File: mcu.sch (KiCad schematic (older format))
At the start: 30 parts, among them Q3 MMBT3904-7-F, SW1 PTS645VL39-2, U4 CAT24C32, U5 STM32F765VIT6, X1 ECS-TXO-3225-200-TR

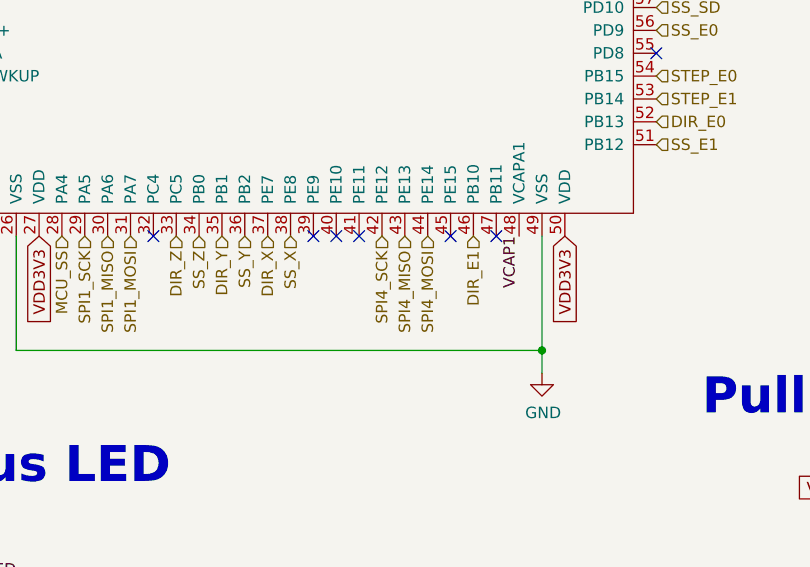
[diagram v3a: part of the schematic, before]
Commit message: Connected TMC DIAG pins to MCU
We had some pins free, so I decided to connect them, so that we
don't need to use the ENDSTOP OVER SPI feature.
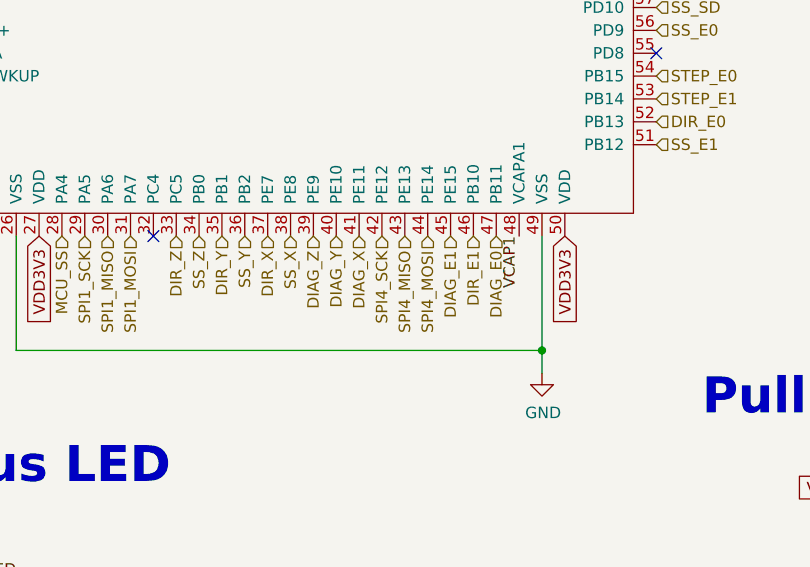
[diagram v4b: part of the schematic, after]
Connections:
- net DIAG_Z: now reaches U5.39 (PE9)
- net DIAG_Y: now reaches U5.40 (PE10)
- net DIAG_X: now reaches U5.41 (PE11)
- net DIAG_E1: now reaches U5.45 (PE15)
- net DIAG_E0: now reaches U5.47 (PB11)
- no-connect marks 25 -> 20
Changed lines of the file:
@@
 SPI1_MOSI
 NoConn ~ 6150 4600
-NoConn ~ 6850 4600
-NoConn ~ 6950 4600
 Text HLabel 6350 4600 3    50   Input ~ 0
 SS_Z
@@
 Text HLabel 7250 4600 3    50   Input ~ 0
 SPI4_MISO
-NoConn ~ 7450 4600
 Text HLabel 7350 4600 3    50   Input ~ 0
 SPI4_MOSI
@@
 DIR_X
 NoConn ~ 8350 3800
-NoConn ~ 7650 4600
 Text HLabel 8350 3500 2    50   Input ~ 0
 SD_DETECT
-NoConn ~ 7050 4600
 Text HLabel 5150 2000 0    50   Input ~ 0
 X_MIN
@@
 Text HLabel 5150 1800 0    50   Input ~ 0
 Z_MIN
-$Comp
-L heteromycin:STM32F765VIT6 U5
-U 1 1 5AD0AB9A
-P 6750 3000
-F 0 "U5" H 6750 3000 50  0000 L CNN
-F 1 "STM32F765VIT6" H 6500 2900 50  0000 L CNN
-F 2 "heteromycin:TQFP-100_14x14mm_P0.5mm" H 6750 3000 50  0001 C CNN
-F 3 "http://www.st.com/en/microcontrollers/stm32f765vi.html" H 6750 3000 50  0001 C CNN
-	1    6750 3000
-	1    0    0    -1
-$EndComp
 Text HLabel 6850 1400 1    50   Input ~ 0
 D1
@@
 	2000 2850 1900 2850
 NoConn ~ 7850 1400
+$Comp
+L heteromycin:STM32F765VIT6 U5
+U 1 1 5AD0AB9A
+P 6750 3000
+F 0 "U5" H 6750 3000 50  0000 L CNN
+F 1 "STM32F765VIT6" H 6500 2900 50  0000 L CNN
+F 2 "heteromycin:TQFP-100_14x14mm_P0.5mm" H 6750 3000 50  0001 C CNN
+F 3 "http://www.st.com/en/microcontrollers/stm32f765vi.html" H 6750 3000 50  0001 C CNN
+	1    6750 3000
+	1    0    0    -1
+$EndComp
+Text HLabel 6850 4600 3    50   Input ~ 0
+DIAG_Z
+Text HLabel 6950 4600 3    50   Input ~ 0
+DIAG_Y
+Text HLabel 7050 4600 3    50   Input ~ 0
+DIAG_X
+Text HLabel 7450 4600 3    50   Input ~ 0
+DIAG_E1
+Text HLabel 7650 4600 3    50   Input ~ 0
+DIAG_E0
 $EndSCHEMATC

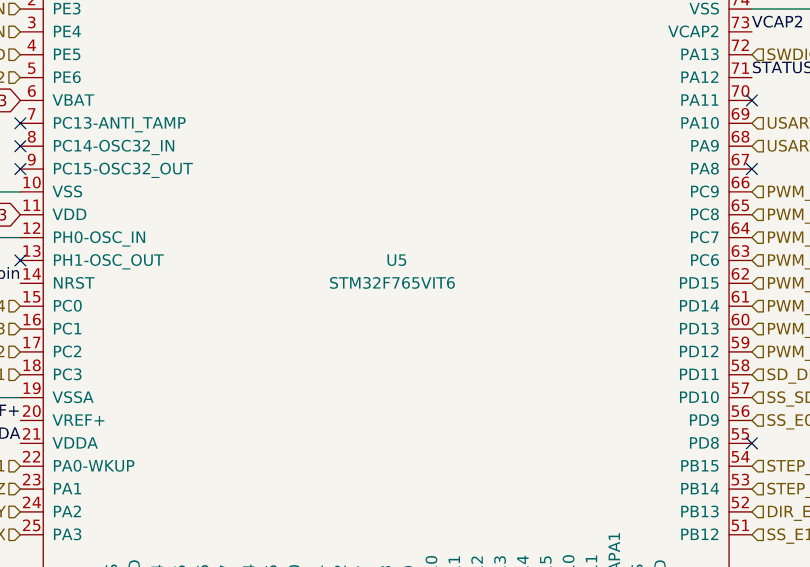
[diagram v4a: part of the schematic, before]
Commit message: Update the MCU from STM32F765VI to STM32H743VI
More speed, more RAM. Only loose the compability to flash over
USART3. Flashing over USART1/I2C/SPI is still possible.
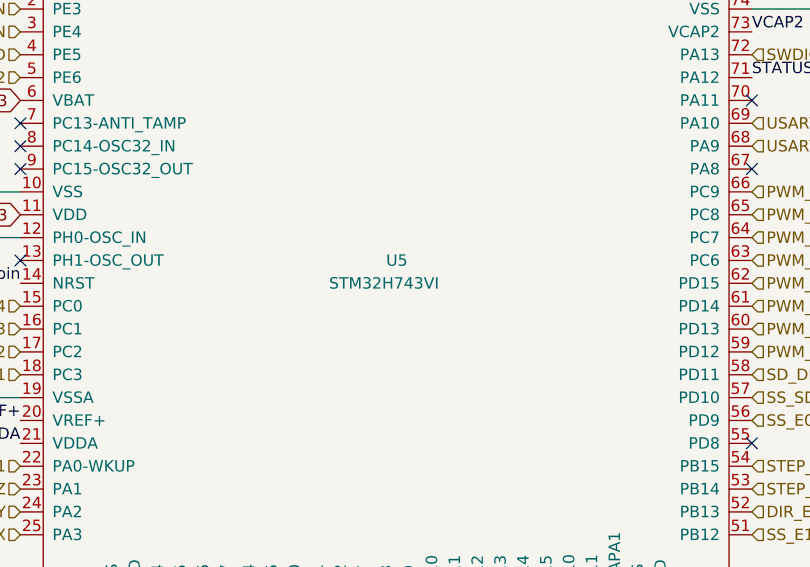
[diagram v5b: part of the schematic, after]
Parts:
- U5: value STM32F765VIT6 -> STM32H743VI
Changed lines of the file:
@@
 P 6750 3000
 F 0 "U5" H 6750 3000 50  0000 L CNN
-F 1 "STM32F765VIT6" H 6500 2900 50  0000 L CNN
+F 1 "STM32H743VI" H 6500 2900 50  0000 L CNN
 F 2 "heteromycin:TQFP-100_14x14mm_P0.5mm" H 6750 3000 50  0001 C CNN
-F 3 "http://www.st.com/en/microcontrollers/stm32f765vi.html" H 6750 3000 50  0001 C CNN
+F 3 "https://www.st.com/en/microcontrollers/stm32h743vi.html" H 6750 3000 50  0001 C CNN
 	1    6750 3000
 	1    0    0    -1

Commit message: Improve Readability
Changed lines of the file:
@@
-$EndComp
-$Comp
-L power:GND #PWR043
-U 1 1 5AF5BF00
-P 4450 3600
-F 0 "#PWR043" H 4450 3350 50  0001 C CNN
-F 1 "GND" V 4455 3472 50  0000 R CNN
-F 2 "" H 4450 3600 50  0001 C CNN
-F 3 "" H 4450 3600 50  0001 C CNN
-	1    4450 3600
-	0    1    1    0
 $EndComp
 $Comp
@@
 $EndComp
 $Comp
-L power:GND #PWR047
-U 1 1 5AF5E7FC
-P 9300 1900
-F 0 "#PWR047" H 9300 1650 50  0001 C CNN
-F 1 "GND" H 9300 1750 50  0000 C CNN
-F 2 "" H 9300 1900 50  0001 C CNN
-F 3 "" H 9300 1900 50  0001 C CNN
-	1    9300 1900
-	0    -1   -1   0
-$EndComp
-$Comp
 L power:GND #PWR046
 U 1 1 5AF5F2E4
@@
 	1    1550 2850
 	1    0    0    -1
-$EndComp
-$Comp
-L power:GND #PWR032
-U 1 1 5AF616AA
-P 1100 2850
-F 0 "#PWR032" H 1100 2600 50  0001 C CNN
-F 1 "GND" H 1105 2677 50  0000 C CNN
-F 2 "" H 1100 2850 50  0001 C CNN
-F 3 "" H 1100 2850 50  0001 C CNN
-	1    1100 2850
-	0    1    1    0
 $EndComp
 Wire Wire Line
@@
 	1450 6500 1800 6500
 Connection ~ 1800 6500
-Connection ~ 1100 2850
 Text GLabel 8350 1800 2    50   Input ~ 0
 VDD3V3
@@
 Wire Wire Line
 	1900 3200 1900 2850
-$Comp
-L power:GND #PWR031
-U 1 1 5AFDE2A1
-P 950 7450
-F 0 "#PWR031" H 950 7200 50  0001 C CNN
-F 1 "GND" H 955 7277 50  0000 C CNN
-F 2 "" H 950 7450 50  0001 C CNN
-F 3 "" H 950 7450 50  0001 C CNN
-	1    950  7450
-	0    1    1    0
-$EndComp
 Text HLabel 4050 2650 2    50   Input ~ 0
 BOOT
@@
 	1    1900 4350
 	1    0    0    -1
-$EndComp
-$Comp
-L power:GND #PWR?
-U 1 1 5BC1FDFA
-P 1300 4250
-AR Path="/5BC1FDFA" Ref="#PWR?"  Part="1"
-AR Path="/5BC4AC32/5BC1FDFA" Ref="#PWR?"  Part="1"
-AR Path="/5BC1C8A4/5BC1FDFA" Ref="#PWR033"  Part="1"
-F 0 "#PWR033" H 1300 4000 50  0001 C CNN
-F 1 "GND" H 1300 4100 50  0000 C CNN
-F 2 "" H 1300 4250 50  0000 C CNN
-F 3 "" H 1300 4250 50  0000 C CNN
-	1    1300 4250
-	0    1    1    0
 $EndComp
 $Comp
@@
 	5650 1400 5650 850
 Wire Wire Line
-	4450 3600 4500 3600
-Wire Wire Line
-	4500 3600 4500 2700
-Wire Wire Line
 	4500 2700 5150 2700
-Connection ~ 4500 3600
 Wire Wire Line
 	4500 3600 5150 3600
@@
 Wire Wire Line
 	950  7150 1150 7150
-Wire Wire Line
-	950  7450 1150 7450
 Connection ~ 1150 7150
 Wire Wire Line
 	1150 7150 1600 7150
-Connection ~ 1150 7450
 Wire Wire Line
 	1150 7450 1600 7450
@@
 Text HLabel 7650 4600 3    50   Input ~ 0
 DIAG_E0
+Wire Wire Line
+	4500 3600 4500 2700
+$Comp
+L power:GND #PWR0138
+U 1 1 5C45B9BC
+P 4500 3600
+F 0 "#PWR0138" H 4500 3350 50  0001 C CNN
+F 1 "GND" H 4505 3427 50  0000 C CNN
+F 2 "" H 4500 3600 50  0001 C CNN
+F 3 "" H 4500 3600 50  0001 C CNN
+	1    4500 3600
+	1    0    0    -1
+$EndComp
+Connection ~ 4500 3600
+$Comp
+L power:GND #PWR0139
+U 1 1 5C45C692
+P 1100 3200
+F 0 "#PWR0139" H 1100 2950 50  0001 C CNN
+F 1 "GND" H 1105 3027 50  0000 C CNN
+F 2 "" H 1100 3200 50  0001 C CNN
+F 3 "" H 1100 3200 50  0001 C CNN
+	1    1100 3200
+	1    0    0    -1
+$EndComp
+Connection ~ 1100 3200
+$Comp
+L power:GND #PWR0140
+U 1 1 5C45CCF1
+P 1300 4550
+F 0 "#PWR0140" H 1300 4300 50  0001 C CNN
+F 1 "GND" H 1305 4377 50  0000 C CNN
+F 2 "" H 1300 4550 50  0001 C CNN
+F 3 "" H 1300 4550 50  0001 C CNN
+	1    1300 4550
+	1    0    0    -1
+$EndComp
+Connection ~ 1300 4550
+$Comp
+L power:GND #PWR0141
+U 1 1 5C45CE8D
+P 1150 7450
+F 0 "#PWR0141" H 1150 7200 50  0001 C CNN
+F 1 "GND" H 1155 7277 50  0000 C CNN
+F 2 "" H 1150 7450 50  0001 C CNN
+F 3 "" H 1150 7450 50  0001 C CNN
+	1    1150 7450
+	1    0    0    -1
+$EndComp
+Connection ~ 1150 7450
+$Comp
+L power:GND #PWR0142
+U 1 1 5C45D233
+P 9300 1900
+F 0 "#PWR0142" H 9300 1650 50  0001 C CNN
+F 1 "GND" H 9305 1727 50  0000 C CNN
+F 2 "" H 9300 1900 50  0001 C CNN
+F 3 "" H 9300 1900 50  0001 C CNN
+	1    9300 1900
+	1    0    0    -1
+$EndComp
 $EndSCHEMATC

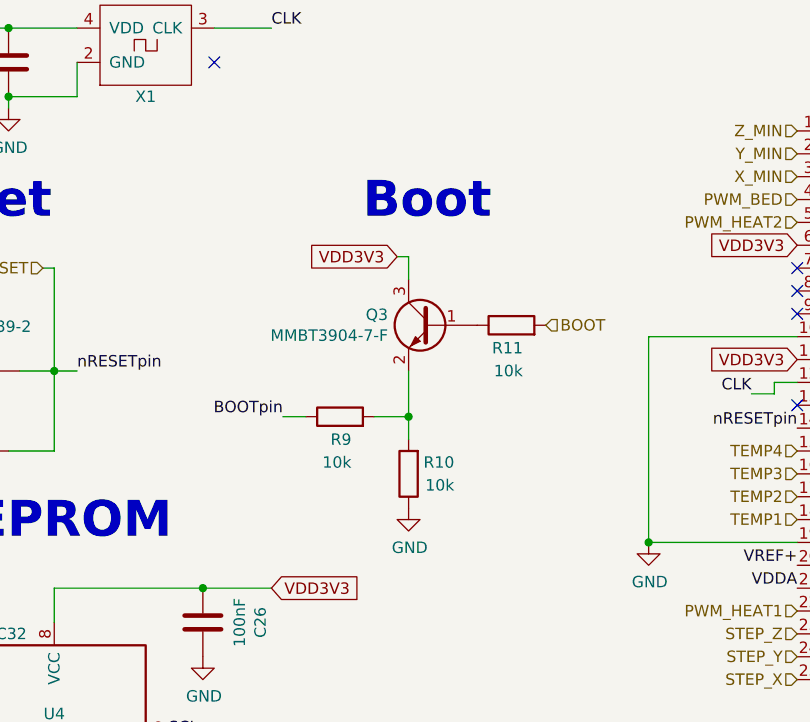
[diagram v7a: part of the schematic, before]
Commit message: Changed boot pin drive interface
Changed the boot pin to a direct connection since the current design depends on a existing raspberry to work. Used a 10kOhms resistor since that's the one used in the development board made by ST
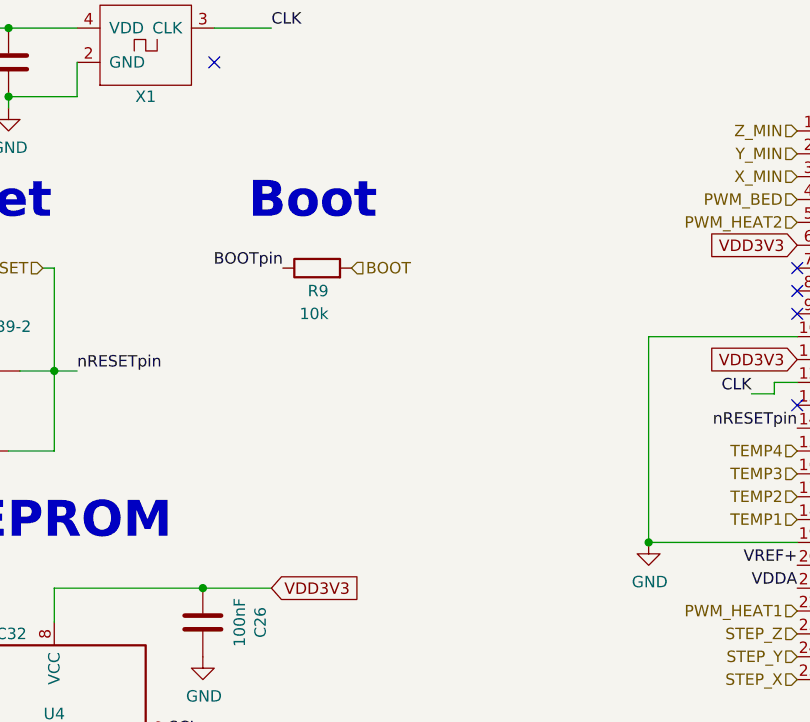
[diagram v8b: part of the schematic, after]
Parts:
- removed Q3: MMBT3904-7-F, Package_TO_SOT_SMD:SOT-23, symbol Device:Q_NPN_BEC
- removed R10, R11: 10k, Resistor_SMD:R_0603_1608Metric, symbol Device:R
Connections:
- net BOOT: now also R9.2
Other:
- moved on the sheet: R9
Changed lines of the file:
@@
 EESchema Schematic File Version 4
 LIBS:heteromycin-cache
-EELAYER 26 0
+EELAYER 29 0
 EELAYER END
 $Descr A4 11693 8268
@@
 Comment4 ""
 $EndDescr
-$Comp
-L Device:R R10
-U 1 1 5AD0B119
-P 3450 3300
-F 0 "R10" H 3250 3250 50  0000 L CNN
-F 1 "10k" H 3250 3350 50  0000 L CNN
-F 2 "Resistor_SMD:R_0603_1608Metric" V 3380 3300 50  0001 C CNN
-F 3 "~" H 3450 3300 50  0001 C CNN
-	1    3450 3300
-	-1   0    0    1
-$EndComp
 Text GLabel 950  6500 0    50   Input ~ 0
 VDD3V3
@@
 	1100 3200 1400 3200
 $Comp
-L power:GND #PWR041
-U 1 1 5AF66D47
-P 3450 3450
-F 0 "#PWR041" H 3450 3200 50  0001 C CNN
-F 1 "GND" H 3455 3277 50  0000 C CNN
-F 2 "" H 3450 3450 50  0001 C CNN
-F 3 "" H 3450 3450 50  0001 C CNN
-	1    3450 3450
-	1    0    0    -1
-$EndComp
-$Comp
 L Device:Ferrite_Bead_Small FB2
 U 1 1 5AF6D789
@@
 Wire Wire Line
 	1900 3200 1900 2850
-Text HLabel 4050 2650 2    50   Input ~ 0
+Text HLabel 3200 2400 2    50   Input ~ 0
 BOOT
 Text Notes 6500 950  0    157  ~ 31
@@
 Text Label 9300 6300 2    50   ~ 0
 SCL
-Text Label 2900 3050 2    50   ~ 0
+Text Label 2900 2400 2    50   ~ 0
 BOOTpin
 $Comp
@@
 L Device:R R9
 U 1 1 5BD6A8E4
-P 3150 3050
-F 0 "R9" V 3050 3000 50  0000 L CNN
-F 1 "10k" V 2950 3000 50  0000 L CNN
-F 2 "Resistor_SMD:R_0603_1608Metric" V 3080 3050 50  0001 C CNN
-F 3 "~" H 3150 3050 50  0001 C CNN
-	1    3150 3050
+P 3050 2400
+F 0 "R9" V 2950 2350 50  0000 L CNN
+F 1 "10k" V 2850 2350 50  0000 L CNN
+F 2 "Resistor_SMD:R_0603_1608Metric" V 2980 2400 50  0001 C CNN
+F 3 "~" H 3050 2400 50  0001 C CNN
+	1    3050 2400
 	0    -1   -1   0
 $EndComp
-Text Notes 3250 2200 0    157  ~ 31
+Text Notes 2750 2200 0    157  ~ 31
 Boot
 Connection ~ 1900 2850
-Wire Wire Line
-	3300 3050 3450 3050
-Text GLabel 3400 2350 0    50   Input ~ 0
-VDD3V3
-$Comp
-L Device:Q_NPN_BEC Q3
-U 1 1 5BD9AD61
-P 3550 2650
-F 0 "Q3" H 3740 2696 50  0000 L CNN
-F 1 "MMBT3904-7-F" H 3740 2605 50  0000 L CNN
-F 2 "Package_TO_SOT_SMD:SOT-23" H 3750 2750 50  0001 C CNN
-F 3 "https://eu.mouser.com/datasheet/2/115/ds30036-41708.pdf" H 3550 2650 50  0001 C CNN
-	1    3550 2650
-	-1   0    0    -1
-$EndComp
-Wire Wire Line
-	3450 3150 3450 3050
-Wire Wire Line
-	3450 2850 3450 3050
-Connection ~ 3450 3050
-Wire Wire Line
-	3400 2350 3450 2350
-Wire Wire Line
-	3450 2350 3450 2450
-Wire Wire Line
-	2900 3050 3000 3050
-$Comp
-L Device:R R11
-U 1 1 5BDA97CE
-P 3900 2650
-F 0 "R11" V 3800 2600 50  0000 L CNN
-F 1 "10k" V 3700 2600 50  0000 L CNN
-F 2 "Resistor_SMD:R_0603_1608Metric" V 3830 2650 50  0001 C CNN
-F 3 "~" H 3900 2650 50  0001 C CNN
-	1    3900 2650
-	0    -1   -1   0
-$EndComp
 Text Label 5150 3100 2    50   ~ 0
 nRESETpin
